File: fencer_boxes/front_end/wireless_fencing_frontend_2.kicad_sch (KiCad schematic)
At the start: 18 parts, among them J1 Conn_01x03, J2 Conn_01x08, U2 AD8619

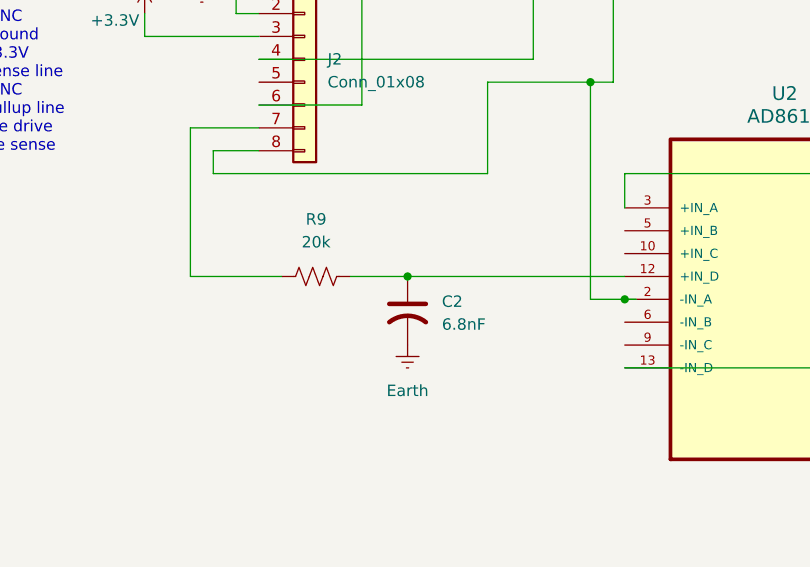
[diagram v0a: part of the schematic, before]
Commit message: fix lame drive component values
not sure these are final (higher f0 than i think is warranted),
but seem to work ok and what i had was bad (i.e. different than
intended and not working...)
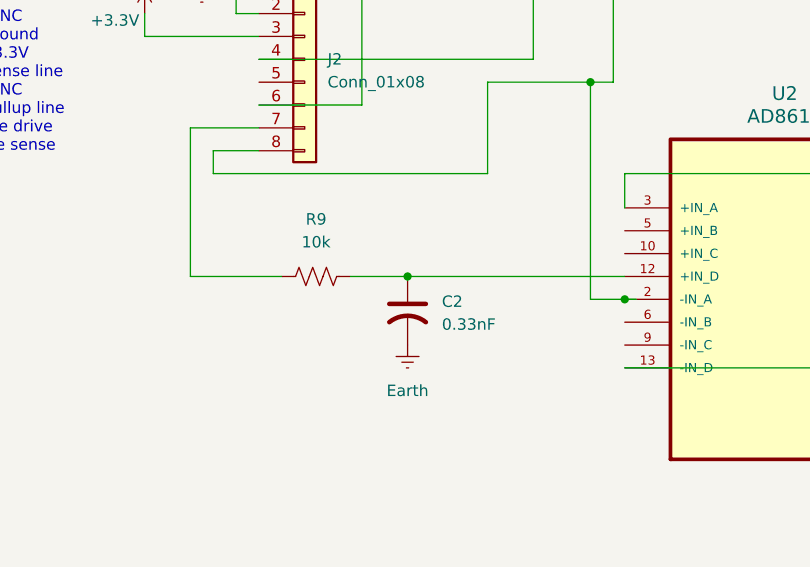
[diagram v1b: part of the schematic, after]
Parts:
- C2: value 6.8nF -> 0.33nF
- R9: value 20k -> 10k
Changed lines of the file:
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@@
 			)
 		)
-		(property "Value" "20k"
+		(property "Value" "10k"
 			(at 97.79 114.3 90)
 			(effects
@@
 			)
 		)
-		(property "Value" "6.8nF"
+		(property "Value" "0.33nF"
 			(at 111.76 123.4439 0)
 			(effects
